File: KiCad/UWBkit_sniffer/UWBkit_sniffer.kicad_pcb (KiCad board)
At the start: 2 copper layers, 40 x 52 mm, 21 parts, among them J1 Conn_Coaxial, J2 Conn_SWD, J3 Conn_GPIO, SW1 SW_Push, U1 LBUA5QJ2AB

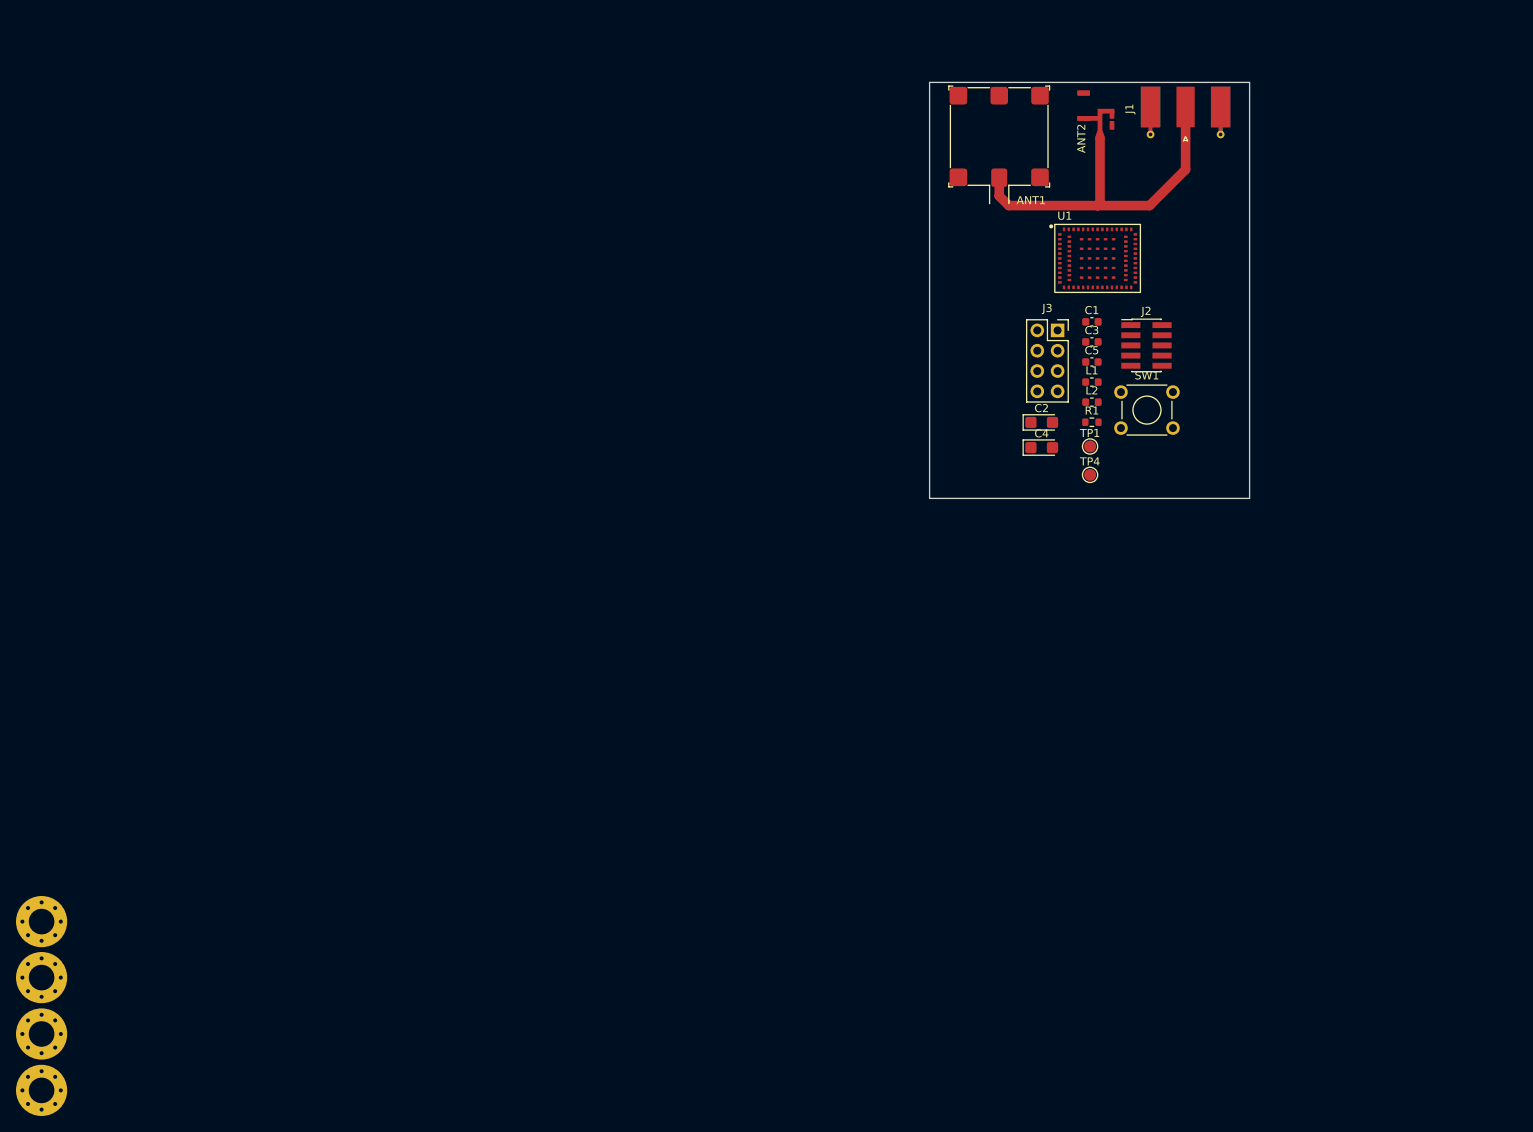
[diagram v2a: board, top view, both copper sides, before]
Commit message: Added components to schematic
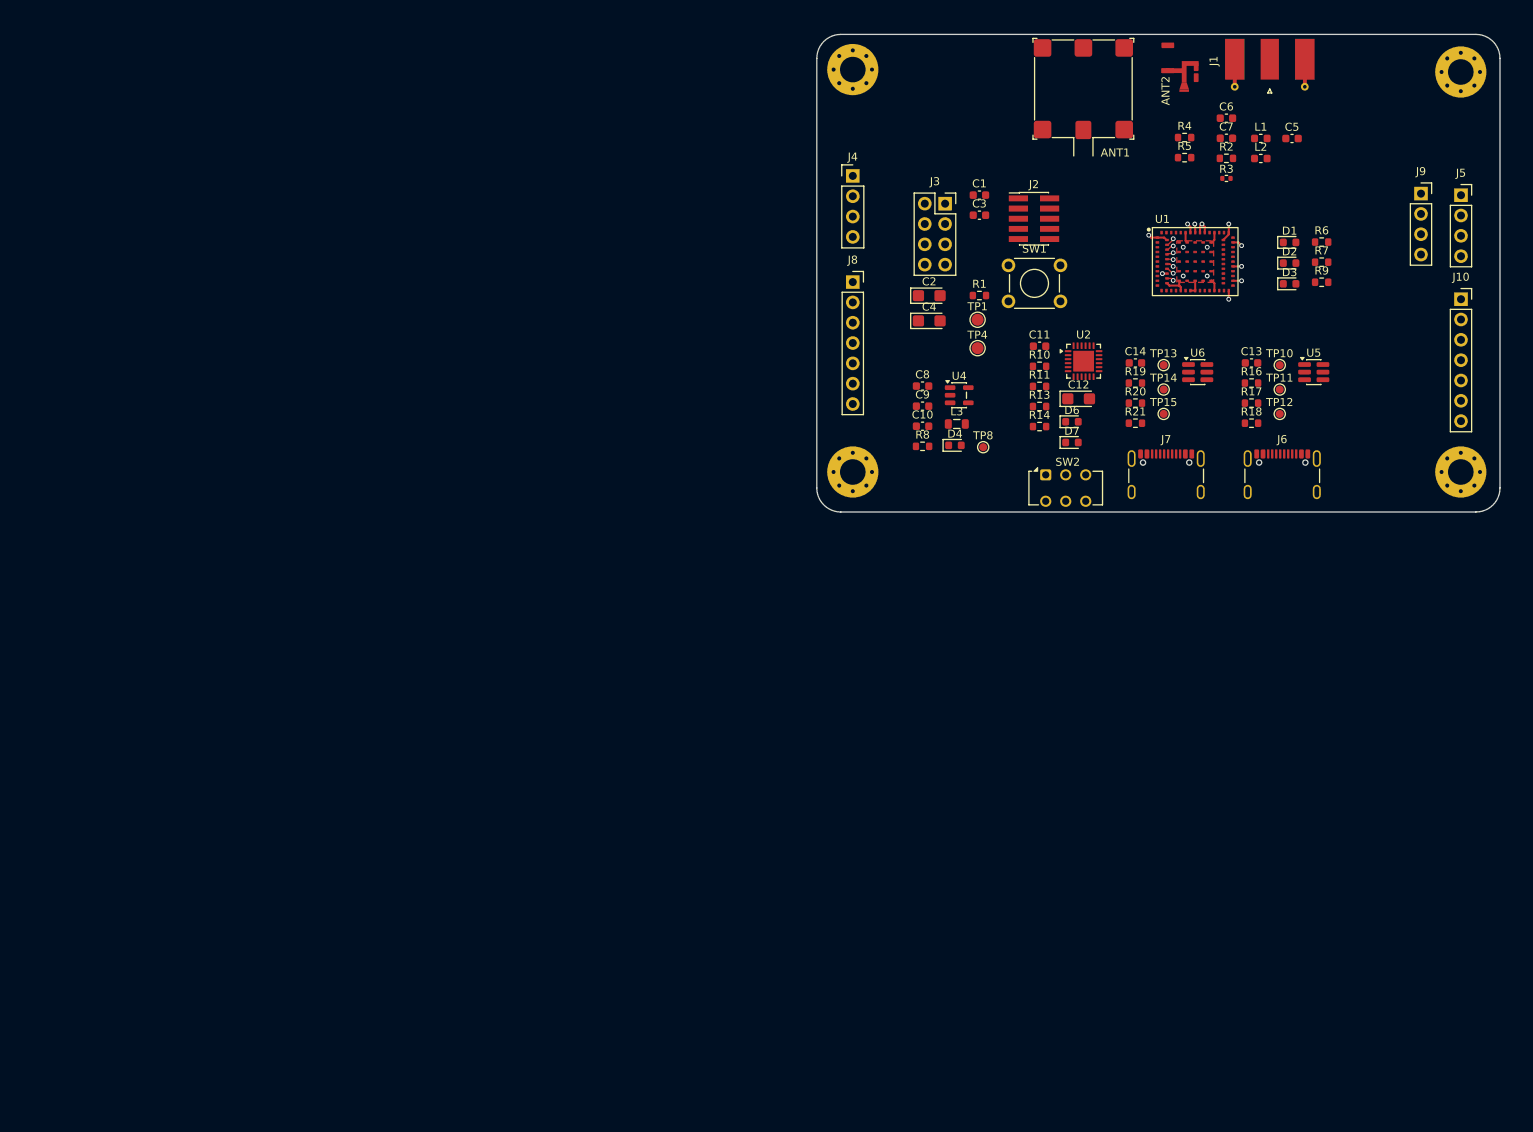
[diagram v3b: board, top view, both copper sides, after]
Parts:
- added C10: 10u, Capacitor_SMD:C_0603_1608Metric, F.Cu at (131.1, 105.0)
- added C11: 100n, Capacitor_SMD:C_0603_1608Metric, F.Cu at (145.7, 95.0)
- added C12: 1u, Capacitor_Tantalum_SMD:CP_EIA-3216-18_Kemet-A, F.Cu at (150.6, 101.5)
- added C13: 100n, Capacitor_SMD:C_0603_1608Metric, F.Cu at (172.2, 97.1)
- added C14: 100n, Capacitor_SMD:C_0603_1608Metric, F.Cu at (157.7, 97.1)
- added C6: C, Capacitor_SMD:C_0603_1608Metric, F.Cu at (169.1, 66.5)
- added C7: C, Capacitor_SMD:C_0603_1608Metric, F.Cu at (169.1, 69.0)
- added C8: 100n, Capacitor_SMD:C_0603_1608Metric, F.Cu at (131.1, 100.0)
- added C9: 10u, Capacitor_SMD:C_0603_1608Metric, F.Cu at (131.1, 102.5)
- added D1: R, LED_SMD:LED_0603_1608Metric, F.Cu at (177.0, 82.0)
- added D2: R, LED_SMD:LED_0603_1608Metric, F.Cu at (177.0, 84.6)
- added D3: G, LED_SMD:LED_0603_1608Metric, F.Cu at (177.0, 87.2)
- added D4: R, LED_SMD:LED_0603_1608Metric, F.Cu at (135.2, 107.4)
- added D6: G, LED_SMD:LED_0603_1608Metric, F.Cu at (149.8, 104.4)
- added D7: R, LED_SMD:LED_0603_1608Metric, F.Cu at (149.8, 107.0)
- added J10: Conn_SPIM, Connector_PinSocket_2.54mm:PinSocket_1x07_P2.54mm_Vertical, F.Cu at (198.4, 89.1)
- added J4: Conn_01x04, Connector_PinHeader_2.54mm:PinHeader_1x04_P2.54mm_Vertical, F.Cu at (122.4, 73.7)
- added J5: Conn_I2C2, Connector_PinSocket_2.54mm:PinSocket_1x04_P2.54mm_Vertical, F.Cu at (198.4, 76.1)
- added J6: USB_C_Receptacle_USB2.0_14P, Connector_USB:USB_C_Receptacle_GCT_USB4105-xx-A_16P_TopMnt_Horizontal, F.Cu at (176.1, 112.1)
- added J7: USB_C_Receptacle_USB2.0_14P, Connector_USB:USB_C_Receptacle_GCT_USB4105-xx-A_16P_TopMnt_Horizontal, F.Cu at (161.6, 112.1)
- added J8: Conn_SPIS, Connector_PinSocket_2.54mm:PinSocket_1x07_P2.54mm_Vertical, F.Cu at (122.4, 87.0)
- added J9: Conn_I2C1, Connector_PinSocket_2.54mm:PinSocket_1x04_P2.54mm_Vertical, F.Cu at (193.4, 75.9)
- added L3: 2.2u, Inductor_SMD:L_0805_2012Metric, F.Cu at (135.4, 104.7)
- added R10: 24k, Resistor_SMD:R_0603_1608Metric, F.Cu at (145.7, 97.5)
- added R11: 47k, Resistor_SMD:R_0603_1608Metric, F.Cu at (145.7, 100.0)
- added R13: 2k1, Resistor_SMD:R_0603_1608Metric, F.Cu at (145.7, 102.5)
- added R14: 3k3, Resistor_SMD:R_0603_1608Metric, F.Cu at (145.7, 105.0)
- added R16: 10k, Resistor_SMD:R_0603_1608Metric, F.Cu at (172.2, 99.6)
- added R17: 5k1, Resistor_SMD:R_0603_1608Metric, F.Cu at (172.2, 102.1)
- added R18: 5k1, Resistor_SMD:R_0603_1608Metric, F.Cu at (172.2, 104.6)
- added R19: 10k, Resistor_SMD:R_0603_1608Metric, F.Cu at (157.7, 99.6)
- added R2: 0R, Resistor_SMD:R_0603_1608Metric, F.Cu at (169.1, 71.5)
- added R20: 5k1, Resistor_SMD:R_0603_1608Metric, F.Cu at (157.7, 102.1)
- added R21: 5k1, Resistor_SMD:R_0603_1608Metric, F.Cu at (157.7, 104.6)
- added R3: 0R, Resistor_SMD:R_0402_1005Metric, F.Cu at (169.1, 74.0)
- added R4: 0R, Resistor_SMD:R_0603_1608Metric, F.Cu at (163.9, 68.9)
- added R5: 0R, Resistor_SMD:R_0603_1608Metric, F.Cu at (163.9, 71.4)
- added R6: 2k1, Resistor_SMD:R_0603_1608Metric, F.Cu at (181.0, 82.0)
- added R7: 3k3, Resistor_SMD:R_0603_1608Metric, F.Cu at (181.0, 84.5)
- added R8: 3k3, Resistor_SMD:R_0603_1608Metric, F.Cu at (131.1, 107.5)
- added R9: 3k3, Resistor_SMD:R_0603_1608Metric, F.Cu at (181.0, 87.0)
- added SW2: SW_Slide_DPDT, Button_Switch_THT:SW_CK_JS202011CQN_DPDT_Straight, F.Cu at (146.5, 111.1)
- added TP10: TestPoint_Small, TestPoint:TestPoint_Pad_D1.0mm, F.Cu at (175.8, 97.3)
- added TP11: TestPoint_Small, TestPoint:TestPoint_Pad_D1.0mm, F.Cu at (175.8, 100.4)
- added TP12: TestPoint_Small, TestPoint:TestPoint_Pad_D1.0mm, F.Cu at (175.8, 103.4)
- added TP13: TestPoint_Small, TestPoint:TestPoint_Pad_D1.0mm, F.Cu at (161.3, 97.3)
- added TP14: TestPoint_Small, TestPoint:TestPoint_Pad_D1.0mm, F.Cu at (161.3, 100.4)
- added TP15: TestPoint_Small, TestPoint:TestPoint_Pad_D1.0mm, F.Cu at (161.3, 103.4)
- added TP8: TestPoint_Small, TestPoint:TestPoint_Pad_D1.0mm, F.Cu at (138.7, 107.6)
- added U2: CP2104, Package_DFN_QFN:QFN-24-1EP_4x4mm_P0.5mm_EP2.6x2.6mm, F.Cu at (151.2, 96.8)
- added U4: XC9285B33CMR-G, Package_TO_SOT_SMD:SOT-23-5, F.Cu at (135.7, 101.1)
- added U5: IP4234CZ6, Package_TO_SOT_SMD:SC-74-6_1.55x2.9mm_P0.95mm, F.Cu at (180.0, 98.2)
- added U6: IP4234CZ6, Package_TO_SOT_SMD:SC-74-6_1.55x2.9mm_P0.95mm, F.Cu at (165.5, 98.2)
- moved H3 214.3 mm to (198.4, 60.7)
- moved H4 193.5 mm to (198.4, 110.7)
- moved H1 147.1 mm to (122.4, 60.4)
- moved H2 119.5 mm to (122.4, 110.7)
- moved C5 37.5 mm to (177.3, 69.0)
- moved L1 37.1 mm to (173.4, 69.0)
- moved L2 37.1 mm to (173.4, 71.5)
- moved C1 21.2 mm to (138.2, 76.1)
- moved C3 21.2 mm to (138.2, 78.6)
- moved J3 21.2 mm to (133.9, 77.2)
- moved R1 21.2 mm to (138.2, 88.6)
- moved TP1 21.2 mm to (138.0, 91.7)
- moved TP4 21.2 mm to (138.0, 95.2)
- moved J2 21.2 mm to (145.1, 79.0)
- moved C2 21.2 mm to (132.0, 88.7)
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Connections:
- net /CPU/nRST renamed /nRST
- ANT1 pad 1: /CPU/ANT1 -> Net-(ANT1-Pad1)
- ANT2 pad 1: /CPU/ANT1 -> Net-(ANT2-Pad1)
- ANT2 pad 3: unconnected-(ANT2-FTE-Pad3) -> Net-(ANT2-FTE)
- J1 pad 1: /CPU/ANT1 -> Net-(J1-In)
- U1 pad 10: unconnected-(U1-P1.13-Pad10) -> /CPU/LED2
- U1 pad 11: unconnected-(U1-P1.12-Pad11) -> /CPU/LED3
- U1 pad 39: /CPU/USB_D+ -> /SOC_D+
- U1 pad 40: /CPU/USB_D- -> /SOC_D-
- U1 pad 48: unconnected-(U1-P1.08-Pad48) -> /CPU/SPIS_RESET
- U1 pad 49: unconnected-(U1-P0.09-Pad49) -> /CPU/SPIM_RESET
- U1 pad 9: unconnected-(U1-P0.03/AIN1-Pad9) -> /CPU/LED1
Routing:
- net /CPU/ANT1: track 44.3 -> 0.00 mm
- net GND: track 0.00 -> 18.3 mm, vias 0 -> 10
- net +3V3: track 0.00 -> 3.62 mm, vias 0 -> 2
- net Net-(J3-Pin_1): track 0.00 -> 1.14 mm, vias 0 -> 1
- net SOC_VBUS: track 0.00 -> 1.10 mm, vias 0 -> 1
- net Net-(J3-Pin_6): track 0.00 -> 1.00 mm, vias 0 -> 1
- net Net-(J3-Pin_2): track 0.00 -> 0.96 mm, vias 0 -> 1
- net Net-(J3-Pin_5): track 0.00 -> 0.90 mm, vias 0 -> 1
- net Net-(J3-Pin_8): track 0.00 -> 0.88 mm, vias 0 -> 1
- net Net-(J3-Pin_3): track 0.00 -> 0.86 mm, vias 0 -> 1
- net Net-(J3-Pin_4): track 0.00 -> 0.80 mm, vias 0 -> 1
- net Net-(J3-Pin_7): track 0.00 -> 0.58 mm, vias 0 -> 1
- added copper zone on F.Cu, net GND
- added copper zone on In1.Cu, net GND
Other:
- board size 40 x 52 mm -> 85.4 x 59.7 mm
- copper layers 2 -> 4

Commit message: First version of PCB
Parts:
- added J11: Conn_01x02, Connector_PinHeader_2.54mm:PinHeader_1x02_P2.54mm_Vertical, F.Cu at (149.4, 80.2)
- added R12: 0R, Resistor_SMD:R_0402_1005Metric, F.Cu at (159.2, 72.8)
- added TP2: TestPoint_Small, TestPoint:TestPoint_Pad_D1.0mm, F.Cu at (154.0, 78.3)
- added TP3: TestPoint_Small, TestPoint:TestPoint_Pad_D1.0mm, F.Cu at (154.8, 84.5)
- C1, C2, C3, C4: moved to B.Cu
- C5, C6, C7: footprint Capacitor_SMD:C_0603_1608Metric -> Capacitor_SMD:C_0402_1005Metric
- L1, L2: footprint Inductor_SMD:L_0603_1608Metric -> Inductor_SMD:L_0402_1005Metric
- R2, R4, R5: footprint Resistor_SMD:R_0603_1608Metric -> Resistor_SMD:R_0402_1005Metric
- TP1, TP4: footprint TestPoint:TestPoint_Pad_D1.5mm -> TestPoint:TestPoint_Pad_D1.0mm
- moved J3 56.4 mm to (184.3, 102.6), turned to 180 degrees
- moved J4 49.8 mm to (156.8, 109.7), turned to 90 degrees
- moved SW2 45.4 mm to (137.8, 66.5), turned to -90 degrees
- moved J6 44.7 mm to (135.6, 93.3), turned to -90 degrees
- moved J7 41.7 mm to (135.6, 79.5), turned to -90 degrees
- moved J8 40.0 mm to (158.8, 103.6), turned to -90 degrees
- moved SW1 38.9 mm to (180.8, 86.9), turned to 180 degrees
- moved C13 38.2 mm to (134.2, 100.1), turned to 180 degrees
- moved U5 37.4 mm to (143.0, 93.3), turned to 90 degrees
- moved R16 34.9 mm to (137.4, 100.1)
- moved TP10 34.7 mm to (141.2, 100.1), turned to -90 degrees
- moved TP4 34.6 mm to (167.8, 77.6)
- moved R17 31.8 mm to (143.0, 89.6)
- moved TP12 31.3 mm to (145.7, 94.8), turned to -90 degrees
- moved TP11 31.3 mm to (145.7, 91.8), turned to -90 degrees
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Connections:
- C6 pad 1: /CPU/ANT1 -> Net-(C6-Pad1)
- R14 pad 1: Net-(U2-TXT/GPIO.0) -> Net-(D7-K)
- R14 pad 2: Net-(D7-K) -> Net-(U2-TXT/GPIO.0)
- R2 pad 2: Net-(ANT2-Pad1) -> Net-(ANT1-Pad1)
- R4 pad 1: /CPU/ANT1 -> Net-(C6-Pad1)
- R4 pad 2: Net-(J1-In) -> Net-(ANT2-Pad1)
- R5 pad 2: Net-(ANT1-Pad1) -> Net-(J1-In)
- R6 pad 1: Net-(D3-K) -> /CPU/LED3
- R6 pad 2: /CPU/LED3 -> Net-(D3-K)
- SW2 pad 1: /USB-C_Connector_1/VBUS -> /USB-C_Connector_2/VBUS
- SW2 pad 2: /USB-C_Connector_1/VBUS -> /USB-C_Connector_2/VBUS
- SW2 pad 3: +5V -> SOC_VBUS
- SW2 pad 4: SOC_VBUS -> +5V
- SW2 pad 5: /USB-C_Connector_2/VBUS -> /USB-C_Connector_1/VBUS
- SW2 pad 6: /USB-C_Connector_2/VBUS -> /USB-C_Connector_1/VBUS
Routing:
- net +3V3: track 3.62 -> 156.0 mm, vias 2 -> 7
- net SOC_VBUS: track 1.10 -> 84.5 mm, vias 1 -> 2
- net +5V: track 0.00 -> 73.2 mm, vias 0 -> 2
- net /USB-C_Connector_1/VBUS: track 0.00 -> 51.2 mm, vias 0 -> 4
- net /nRST: track 0.00 -> 42.1 mm, vias 0 -> 7
- net Net-(J3-Pin_2): track 0.96 -> 37.4 mm
- net Net-(J3-Pin_1): track 1.14 -> 35.8 mm
- net /CPU/I2C2_SDA: track 0.00 -> 34.5 mm, vias 0 -> 2
- net Net-(J3-Pin_4): track 0.80 -> 34.6 mm
- net /USB-C_Connector_2/VBUS: track 0.00 -> 33.1 mm, vias 0 -> 2
- net /CPU/I2C2_SCL: track 0.00 -> 32.3 mm, vias 0 -> 1
- net Net-(J3-Pin_3): track 0.86 -> 32.8 mm
- net /CPU/SPIS_CS: track 0.00 -> 30.5 mm
- net Net-(J3-Pin_6): track 1.00 -> 31.0 mm
- net Net-(J3-Pin_5): track 0.90 -> 29.1 mm
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- added copper zone on B.Cu, net GND
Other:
- board size 85.4 x 59.7 mm -> 57.4 x 57.4 mm
- board text added: "FTE"

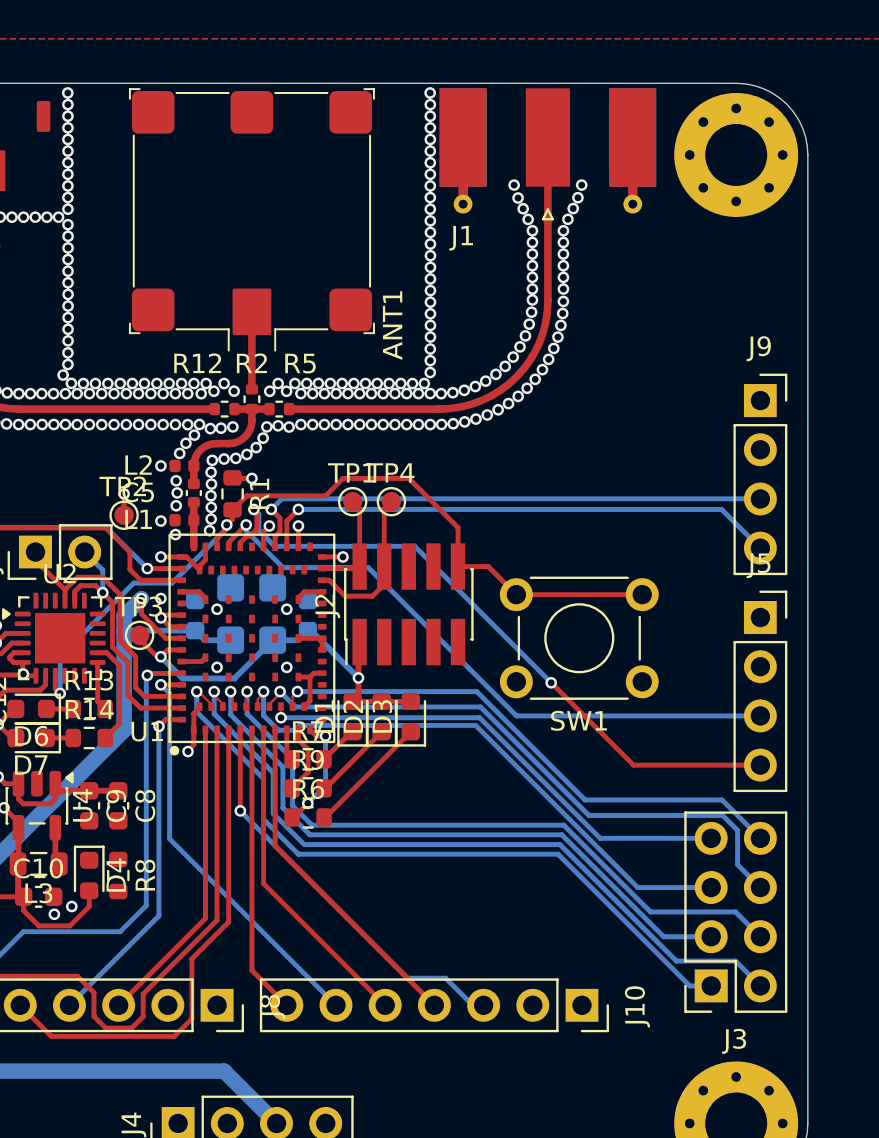
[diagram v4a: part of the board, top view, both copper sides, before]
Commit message: Modified layout, uncovered RF traces
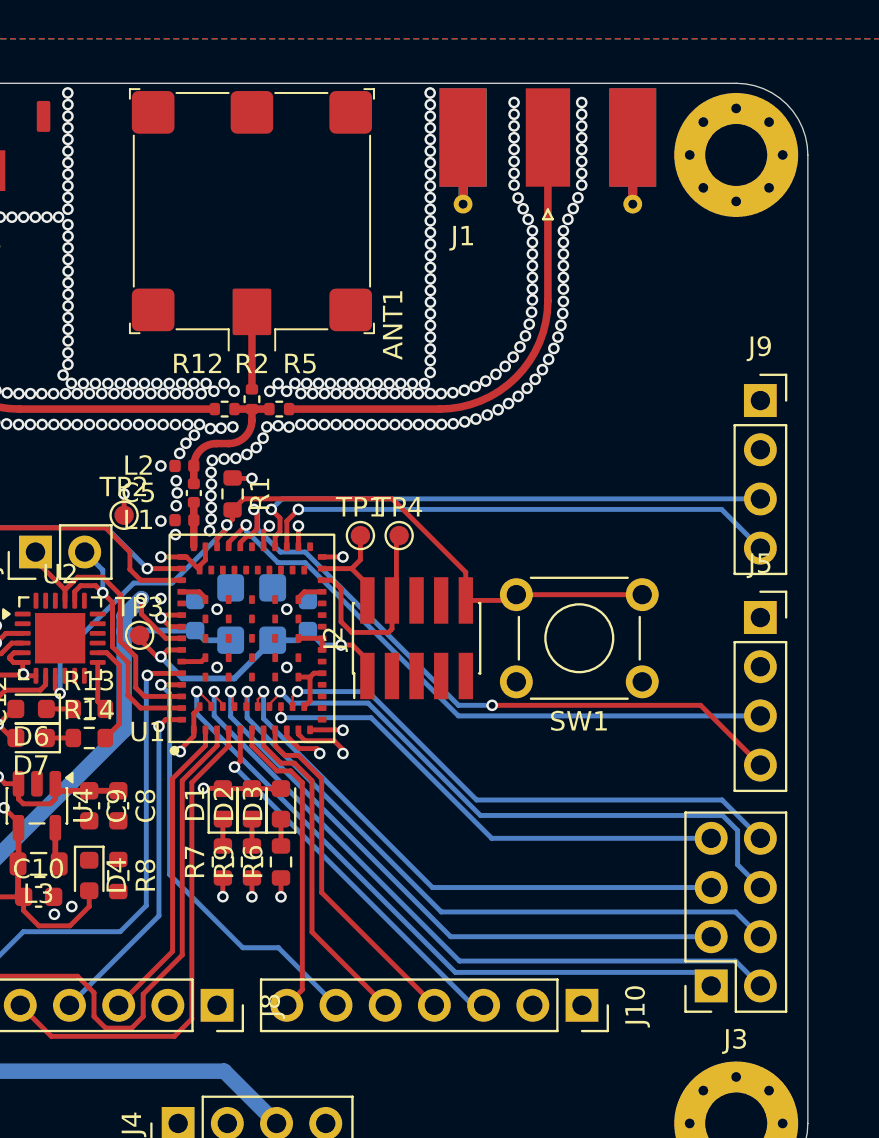
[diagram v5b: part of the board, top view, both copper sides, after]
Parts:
- moved D1 8.07 mm to (159.1, 93.2)
- moved D2 8.07 mm to (160.6, 93.2)
- moved D3 8.07 mm to (162.1, 93.2)
- moved R7 6.89 mm to (159.1, 96.2), turned to 90 degrees
- moved R9 4.78 mm to (160.6, 96.2), turned to 90 degrees
- moved R6 2.69 mm to (162.1, 96.2), turned to 90 degrees
- moved J2 1.80 mm to (169.1, 84.7)
- moved TP1 1.80 mm to (166.2, 79.3)
- moved TP4 1.80 mm to (168.2, 79.3)
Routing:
- net /CPU/LED1: track 1.63 -> 12.9 mm, vias 0 -> 2
- net /CPU/LED2: track 3.57 -> 13.4 mm, vias 0 -> 2
- net /CPU/LED3: track 5.90 -> 13.2 mm
- net +3V3: track 156.0 -> 162.6 mm, vias 7 -> 8
- net Net-(D3-K): track 6.30 -> 1.39 mm
- net Net-(D2-K): track 4.18 -> 1.39 mm
- net /CPU/SWCLK: track 8.22 -> 10.8 mm
- net Net-(J3-Pin_4): track 34.6 -> 33.3 mm
- net Net-(J3-Pin_3): track 32.8 -> 31.7 mm
- net Net-(J3-Pin_1): track 35.8 -> 34.7 mm
- net Net-(J3-Pin_2): track 37.4 -> 36.2 mm
- net /CPU/SPIM_RESET: track 21.4 -> 22.4 mm
- net /CPU/SPIM_CS: track 15.0 -> 16.0 mm
- net /nRST: track 42.1 -> 41.2 mm, vias 7 -> 2
- net /CPU/SPIM_CLK: track 20.9 -> 20.0 mm
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- added copper zone on In2.Cu, net GND
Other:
- board text added: "PCB3D_BR_sniffer"
- board text added: "PCB3D_TL_sniffer"
